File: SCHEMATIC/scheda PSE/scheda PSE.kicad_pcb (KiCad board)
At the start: 2 copper layers, 102.4 x 77.4 mm, 125 parts, among them J1 Conn_01x03, J2 Vin, J3 USB_B_Mini, J4 Vout 5V, J5 I2C_3V3, J6 UART0_3V3, Q1 IRLML0060TRPBF, Q2 PDTC114YT, Q3 IRLML9301, SW1 RESET_SW, SW2 PROG_SW, SW3 SW_U, SW4 SW_L, SW5 SW_R, SW6 SW_D, SW7 Power_button, U1 RP2040, U2 W25Q16JVUSSQ, U3 AT24C256, U4 oled_0.96"_128x64px, U5 TPS563201, U6 XC6705A331MR-G, U7 SAM-M8Q, U8 MMA8451Q, U9 TC1047A, Y1 12MHz

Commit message: finito lo sbroglio (magari da ricontrollare)
finito lo sbroglio, controllato già io ma meglio ridare una controllata.
Da sistemare tutta la serigrafia
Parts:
- moved D10 23.5 mm to (164.4, 77.4), turned to -135 degrees
- moved R12 19.1 mm to (162.1, 79.7), turned to 45 degrees
- moved U7 2.04 mm to (163.1, 115.7), turned to 180 degrees
- moved C19 1.73 mm to (155.5, 74.6)
- moved C20 1.67 mm to (154.2, 73.4)
- moved R7 1.45 mm to (160.1, 88.4)
- moved C9 0.08 mm to (164.0, 86.3)
- moved C14 0.05 mm to (165.3, 85.0)
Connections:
- Q3 pad 1: /RP2040/SAM_EN -> /RP2040/GPS_EN
- R21 pad 2: /RP2040/SAM_EN -> /RP2040/GPS_EN
- U1 pad 11: /Interfaccia utente/BUZZER -> unconnected-(U1-Pad11)
- U1 pad 12: /Interfaccia utente/BUTTON_U -> unconnected-(U1-Pad12)
- U1 pad 13: /Interfaccia utente/BUTTON_D -> /RP2040/ACC_SA0
- U1 pad 14: /Interfaccia utente/BUTTON_L -> /Alimentazione/5V_EN
- U1 pad 15: /Interfaccia utente/BUTTON_R -> /RP2040/GPS_RST
- U1 pad 29: unconnected-(U1-Pad29) -> /RP2040/GPS_EN
- U1 pad 30: unconnected-(U1-Pad30) -> /RP2040/GPS_PPS
- U1 pad 31: /RP2040/SAM_EN -> /Interfaccia utente/LED_ALIVE
- U1 pad 32: unconnected-(U1-Pad32) -> /Interfaccia utente/BUZZER
- U1 pad 34: unconnected-(U1-Pad34) -> /Interfaccia utente/BUTTON_U
- U1 pad 35: unconnected-(U1-Pad35) -> /Interfaccia utente/BUTTON_D
- U1 pad 36: unconnected-(U1-Pad36) -> /Interfaccia utente/BUTTON_R
- U1 pad 37: unconnected-(U1-Pad37) -> /Interfaccia utente/BUTTON_L
- U1 pad 38: unconnected-(U1-Pad38) -> /RP2040/TEMP_SENS
- U1 pad 4: /Alimentazione/5V_EN -> unconnected-(U1-Pad4)
- U1 pad 41: /RP2040/TEMP_SENS -> unconnected-(U1-Pad41)
- U1 pad 5: /Interfaccia utente/LED_ALIVE -> unconnected-(U1-Pad5)
- U1 pad 9: /Interfaccia utente/LED_ALIVE -> unconnected-(U1-Pad9)
- U7 pad 18: unconnected-(U7-Pad18) -> /RP2040/GPS_RST
- U7 pad 7: unconnected-(U7-Pad7) -> /RP2040/GPS_PPS
- U8 pad 7: GND -> /RP2040/ACC_SA0
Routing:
- net /UART0_TX: track 7.67 -> 58.4 mm
- net /UART0_RX: track 7.69 -> 58.4 mm
- net /Alimentazione/5V_EN: track 0.00 -> 41.7 mm, vias 0 -> 2
- net /RP2040/GPS_RST: track 0.00 -> 40.5 mm
- net /UART_TX: track 0.00 -> 38.8 mm
- net /Led_RGB_WS2812B/DIN: track 0.00 -> 38.6 mm, vias 0 -> 2
- net /UART_RX: track 0.00 -> 36.1 mm
- net /Interfaccia utente/BUZZER: track 0.00 -> 35.0 mm, vias 0 -> 2
- net /RP2040/GPS_PPS: track 0.00 -> 35.0 mm, vias 0 -> 2
- net /RP2040/GPS_EN: track 0.00 -> 32.3 mm, vias 0 -> 2
- net /Interfaccia utente/BUTTON_D: track 29.3 -> 57.7 mm, vias 0 -> 2
- net /I2C0_SCL: track 60.4 -> 87.6 mm, vias 0 -> 1
- net /Interfaccia utente/BUTTON_R: track 43.2 -> 68.5 mm, vias 0 -> 2
- net /I2C0_SDA: track 58.6 -> 81.5 mm, vias 0 -> 2
- net /Interfaccia utente/BUTTON_U: track 37.9 -> 59.9 mm, vias 0 -> 2
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
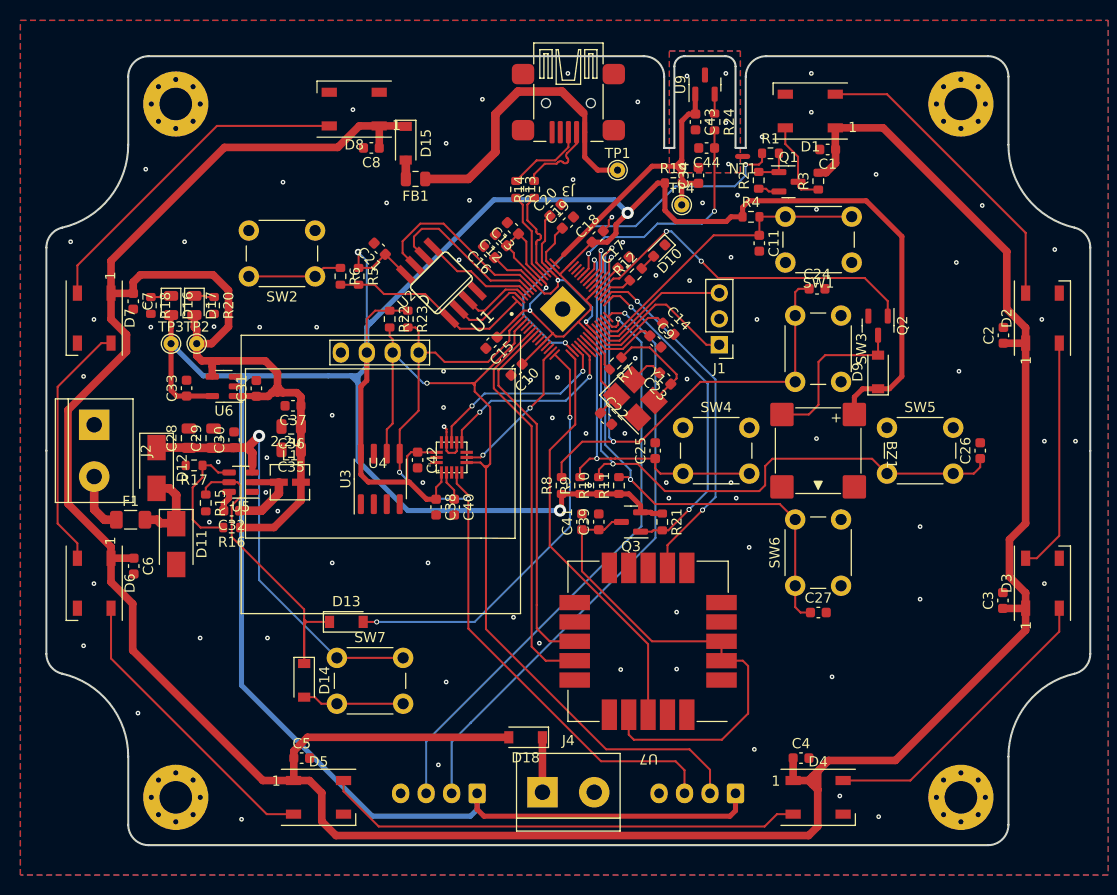
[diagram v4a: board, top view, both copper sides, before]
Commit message: finito tutto
sistemati tutti i nomi dei componenti e inserite tutte le grafiche necessarie
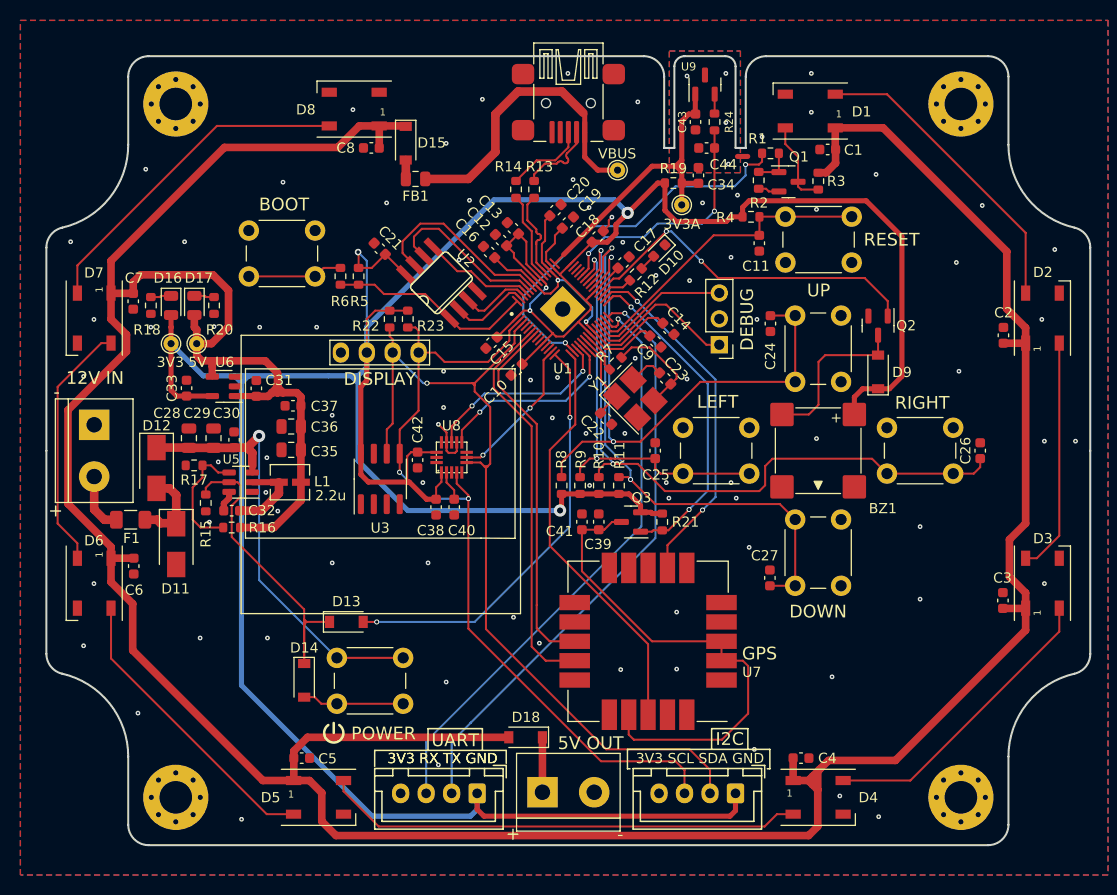
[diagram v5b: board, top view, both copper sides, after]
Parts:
- moved C27 5.84 mm to (175.3, 109.5), turned to 90 degrees
- moved C24 5.71 mm to (175.3, 84.5), turned to -90 degrees
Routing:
- net /Interfaccia utente/BUTTON_U: track 59.9 -> 58.5 mm
- net /Interfaccia utente/BUTTON_D: track 57.7 -> 56.4 mm
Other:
- board text added: "+"
- board text added: "-"
- board text added: "12V IN"
- board text added: "3V3"
- board text added: "3V3 RX TX GND"
- board text added: "3V3 SCL SDA GND"
- board text added: "3V3A"
- board text added: "5V"
- board text added: "5V OUT"
- board text added: "ANNO ACCADEMICO 2022/2023"
- board text added: "BOOT"
- board text added: "CORSO DI PROGETTAZIONE E PROTOTIPAZIONE DI SISTEMI ELETTRONICI"
- board text added: "DEBUG"
- board text added: "DISPLAY"
- board text added: "DOWN"
- board text added: "GPS"
- board text added: "I2C"
- board text added: "LEFT"
- board text added: "POWER"
- board text added: "RESET"
- board text added: "RIGHT"
- board text added: "UART"
- board text added: "UP"
- board text added: "VBUS"

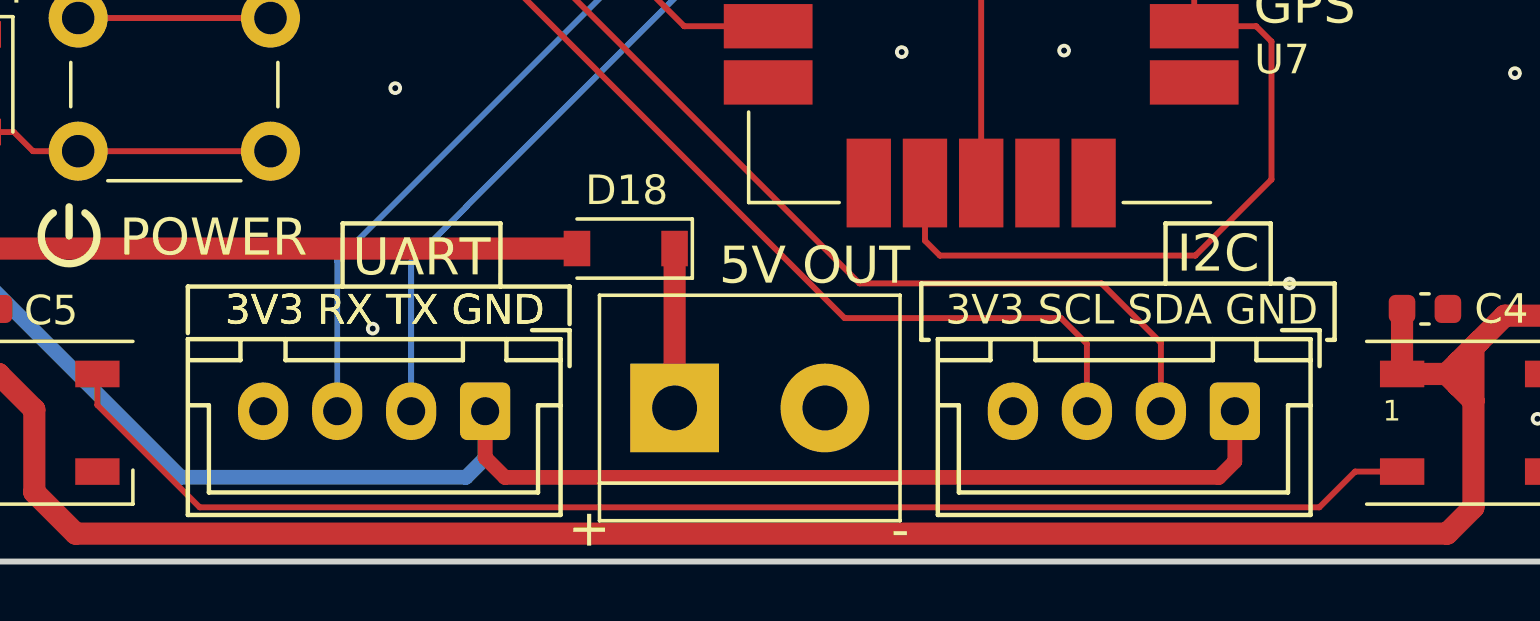
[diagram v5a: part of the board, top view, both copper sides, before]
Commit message: sistemato nomi periferiche esterne uart e i2c
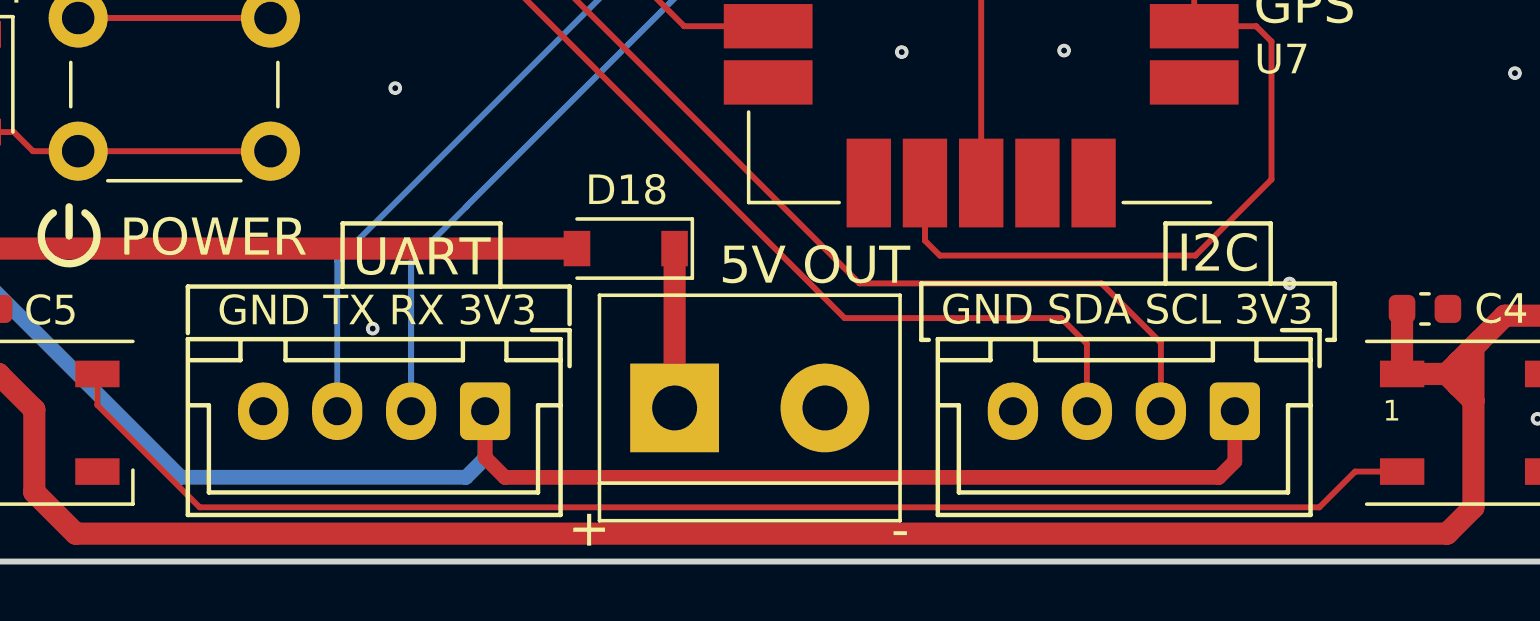
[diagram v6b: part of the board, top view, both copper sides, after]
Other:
- board text added: "GND SDA SCL 3V3"
- board text added: "GND TX RX 3V3"
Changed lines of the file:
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@@
     (effects (font (size 1.25 1.25) (thickness 0.25)) (justify mirror))
-  )
-  (gr_text "3V3 RX TX GND" (at 142.755342 127.182878) (layer "B.SilkS")
-    (effects (font (size 1 1) (thickness 0.15)) (justify mirror))
   )
   (gr_text "5V OUT" (at 155.506142 125.430278) (layer "B.SilkS")
@@
     (effects (font (size 1.25 1.25) (thickness 0.25)))
   )
-  (gr_text "3V3 RX TX GND" (at 143.161742 127.182878) (layer "F.SilkS")
+  (gr_text "GND TX RX 3V3" (at 142.907742 127.208278) (layer "F.SilkS")
     (effects (font (size 1 1) (thickness 0.15)))
   )
@@
     (effects (font (size 1.25 1.25) (thickness 0.25)))
   )
-  (gr_text "3V3 SCL SDA GND" (at 168.409342 127.182878) (layer "F.SilkS")
+  (gr_text "GND SDA SCL 3V3" (at 168.256942 127.182878) (layer "F.SilkS")
     (effects (font (size 1 1) (thickness 0.15)))
   )
@@
     (effects (font (size 1.25 1.25) (thickness 0.25)))
   )
-  (gr_text "3V3 RX TX GND" (at 143.161742 127.182878) (layer "F.SilkS")
-    (effects (font (size 1 1) (thickness 0.15)))
-  )
   (gr_text "-" (at 105.315742 91.241878) (layer "F.SilkS")

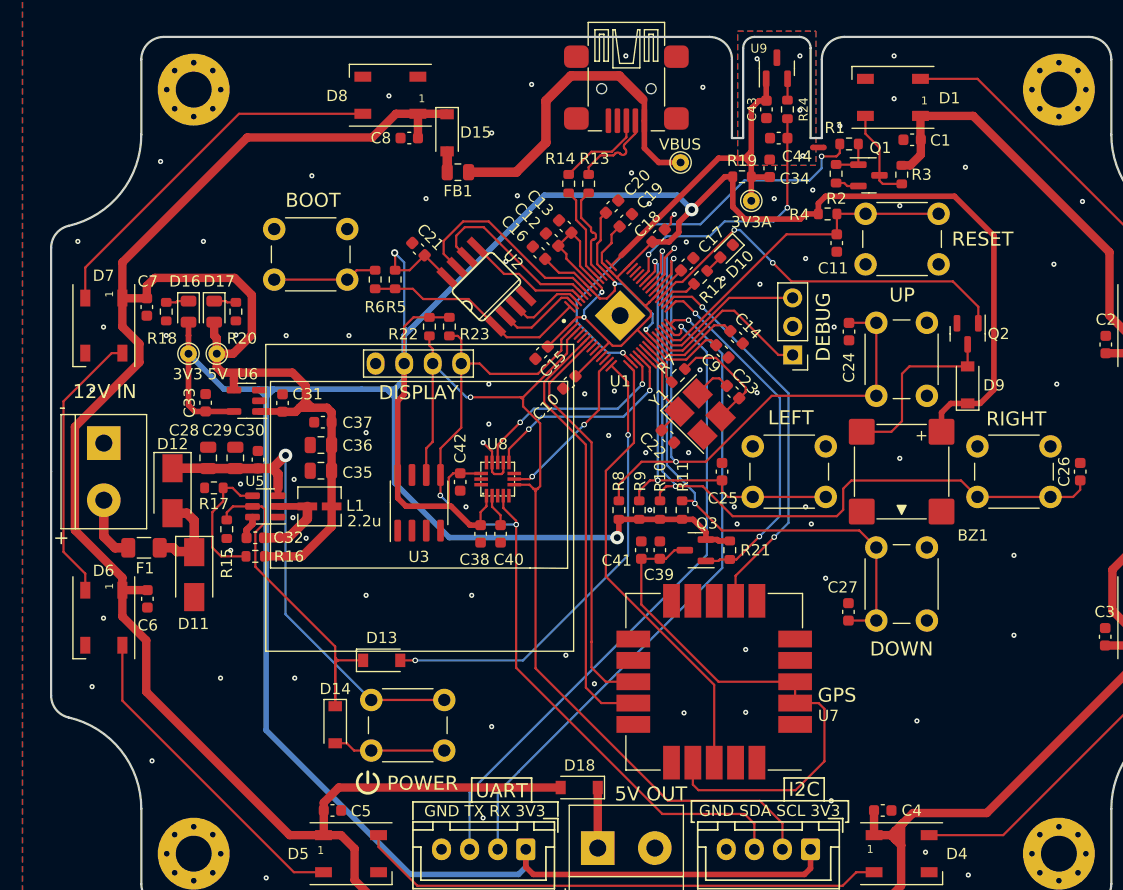
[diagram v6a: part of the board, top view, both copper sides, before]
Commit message: abbellita un po' la scheda
sostituite alcune scritte sulla sceda
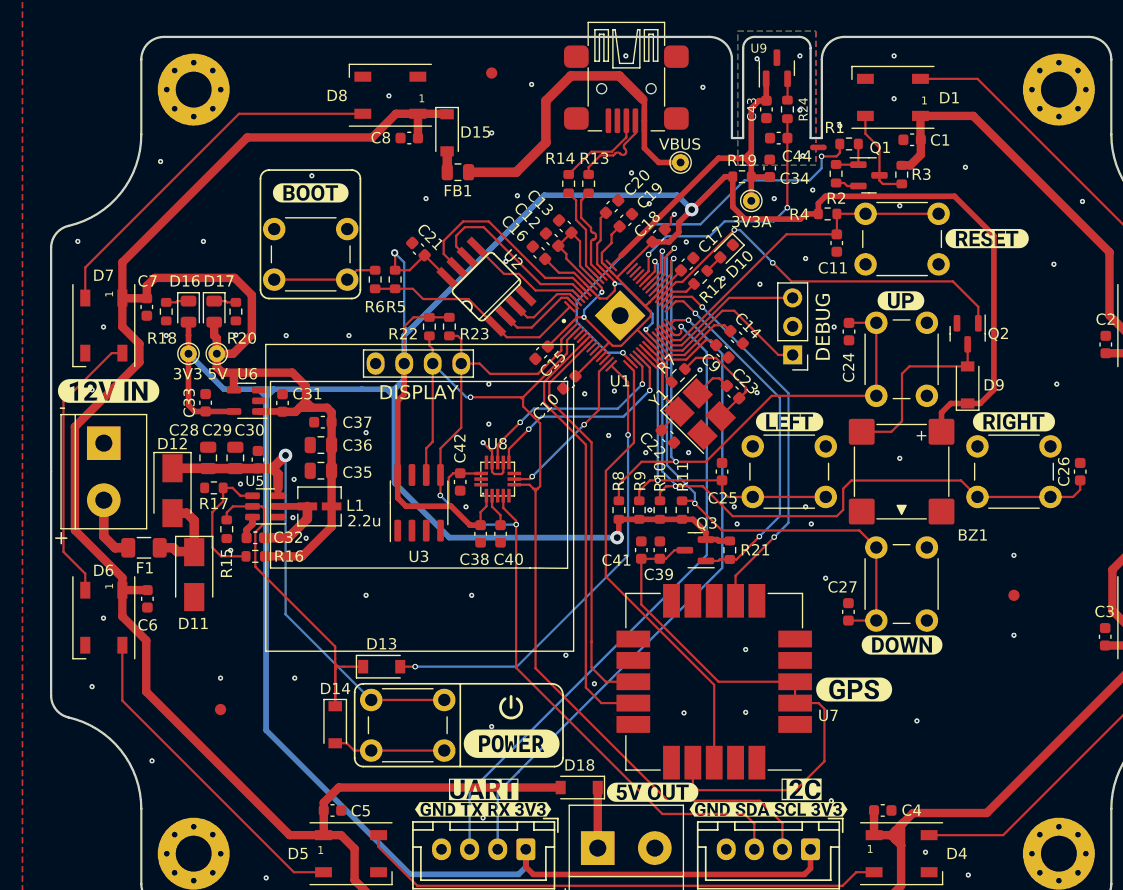
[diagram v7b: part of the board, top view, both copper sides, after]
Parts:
- added REF**: Fiducial_1mm_Mask2mm, Fiducial:Fiducial_1mm_Mask2mm, F.Cu at (190.0, 108.0)
- added REF**: Fiducial_1mm_Mask2mm, Fiducial:Fiducial_1mm_Mask2mm, F.Cu at (119.4, 118.2)
- added REF**: Fiducial_1mm_Mask2mm, Fiducial:Fiducial_1mm_Mask2mm, F.Cu at (143.5, 61.5)
- added kibuzzard-643CF430: G***, kibuzzard-643CF430, F.Cu at (145.3, 121.2)
- added kibuzzard-643CF710: G***, kibuzzard-643CF710, F.Cu at (142.8, 127.1)
- added kibuzzard-643CF7B7: G***, kibuzzard-643CF7B7, F.Cu at (142.8, 125.3)
- added kibuzzard-643CF7B7: G***, kibuzzard-643CF7B7, B.Cu at (142.8, 125.3)
- added kibuzzard-643CF7E4: G***, kibuzzard-643CF7E4, F.Cu at (168.2, 127.1)
- added kibuzzard-643CF80B: G***, kibuzzard-643CF80B, F.Cu at (171.1, 125.3)
- added kibuzzard-643CF80B: G***, kibuzzard-643CF80B, B.Cu at (168.2, 125.3)
- added kibuzzard-643CF88B: G***, kibuzzard-643CF88B, B.Cu at (168.2, 127.1)
- added kibuzzard-643CF8F2: G***, kibuzzard-643CF8F2, B.Cu at (142.8, 127.1)
- added kibuzzard-643CF960: G***, kibuzzard-643CF960, F.Cu at (190.0, 92.6)
- added kibuzzard-643CF96E: G***, kibuzzard-643CF96E, F.Cu at (180.0, 112.4)
- added kibuzzard-643CF993: G***, kibuzzard-643CF993, F.Cu at (170.0, 92.6)
- added kibuzzard-643CF9A0: G***, kibuzzard-643CF9A0, F.Cu at (179.9, 81.8)
- added kibuzzard-643CF9B2: G***, kibuzzard-643CF9B2, F.Cu at (187.6, 76.3)
- added kibuzzard-643CF9C9: G***, kibuzzard-643CF9C9, F.Cu at (127.4, 72.2)
- added kibuzzard-643CFA52: G***, kibuzzard-643CFA52, F.Cu at (157.8, 125.5)
- added kibuzzard-643CFA52: G***, kibuzzard-643CFA52, B.Cu at (155.6, 125.5)
- added kibuzzard-643CFABC: G***, kibuzzard-643CFABC, F.Cu at (109.4, 89.8)
- added kibuzzard-643CFABC: G***, kibuzzard-643CFABC, B.Cu at (114.2, 97.1)
- added kibuzzard-643CFBDA: G***, kibuzzard-643CFBDA, F.Cu at (175.8, 116.4)
- moved D13 0.56 mm to (133.7, 114.4)
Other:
- board text removed: "12V IN"
- board text removed: "3V3 RX TX GND"
- board text removed: "3V3 SCL SDA GND"
- board text removed: "5V OUT"
- board text removed: "BOOT"
- board text removed: "DOWN"
- board text removed: "GND SDA SCL 3V3"
- board text removed: "GND TX RX 3V3"
- board text removed: "GPS"
- board text removed: "I2C"
- board text removed: "LEFT"
- board text removed: "POWER"
- board text removed: "RESET"
- board text removed: "RIGHT"
- board text removed: "UART"
- board text removed: "UP"
